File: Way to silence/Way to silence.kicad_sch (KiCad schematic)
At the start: 1 part, among them U1 ESP32-WROOM-32-N16

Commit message: [DRC] Working on BMS Sheet
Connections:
- no-connect marks 14 -> 17
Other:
- sheet Battery Management ports: added BAT, VIN, VOUT; removed none
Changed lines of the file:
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@@
   (paper "A4")
   (no_connect (at 120.65 71.12))
+  (no_connect (at 82.55 58.42))
   (no_connect (at 120.65 66.04))
   (no_connect (at 120.65 68.58))
@@
   (no_connect (at 199.39 55.88))
   (no_connect (at 176.53 90.17))
+  (no_connect (at 82.55 63.5))
   (no_connect (at 199.39 58.42))
   (no_connect (at 176.53 87.63))
+  (no_connect (at 82.55 60.96))
   (no_connect (at 199.39 66.04))
   (symbol (lib_id "power:PWR_FLAG") (at 177.8 25.4 0) (unit 1)
@@
       (effects (font (size 1.27 1.27)) (justify left top))
     )
-    (instances
+    (pin "VIN" bidirectional (at 82.55 58.42 180)
+      (effects (font (size 1.27 1.27)) (justify left))
+    )
+    (pin "VOUT" bidirectional (at 82.55 60.96 180)
+      (effects (font (size 1.27 1.27)) (justify left))
+    )
+    (pin "BAT" bidirectional (at 82.55 63.5 180)
+      (effects (font (size 1.27 1.27)) (justify left))
+    )
+    (instances

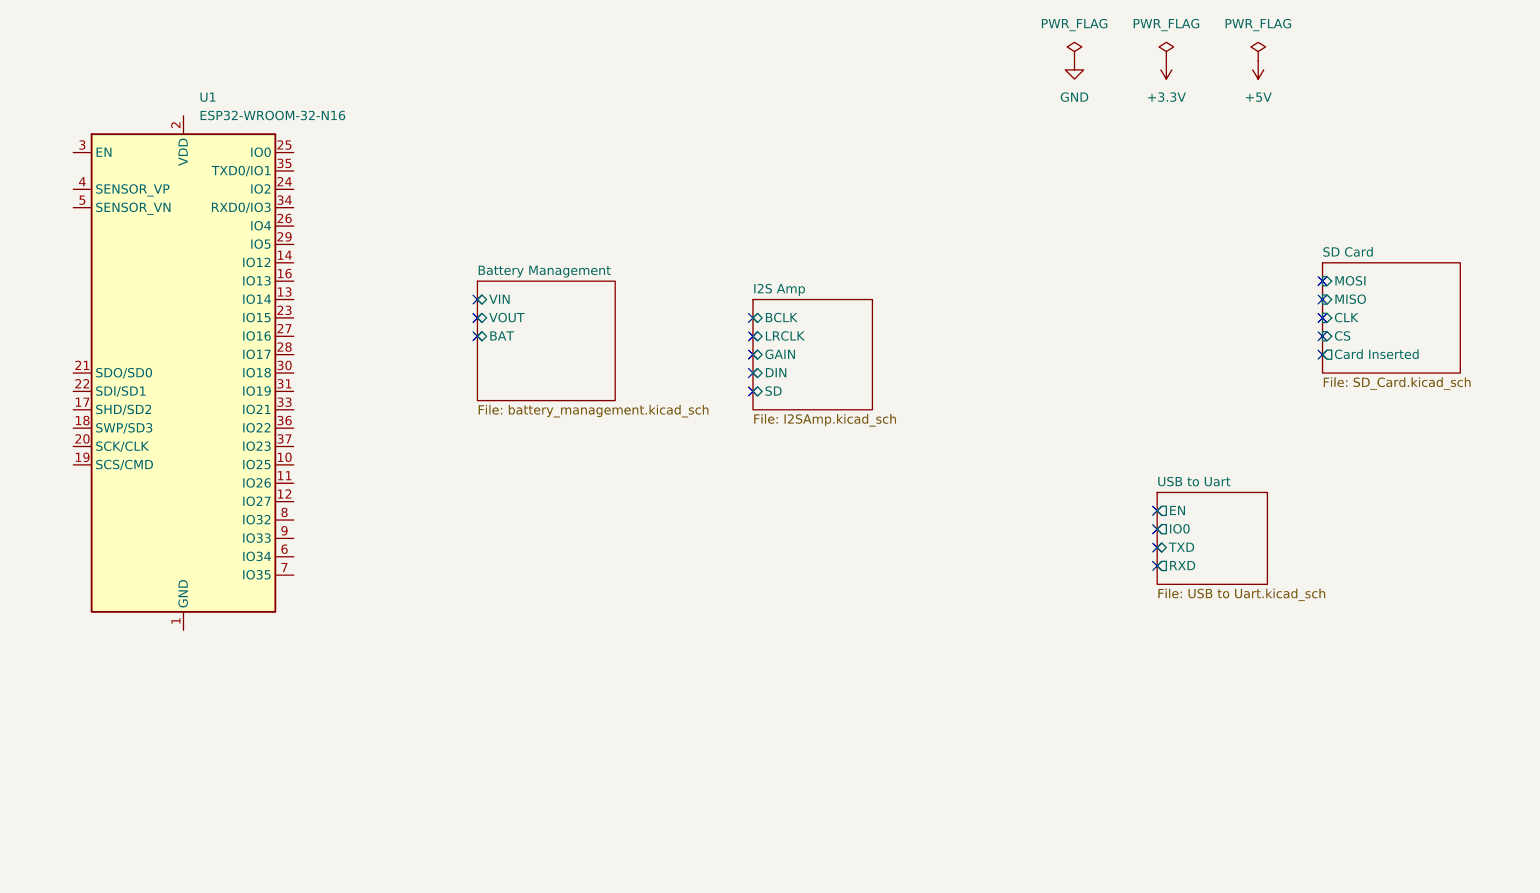
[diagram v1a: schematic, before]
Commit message: [ADD] Completed some connections in main sheet
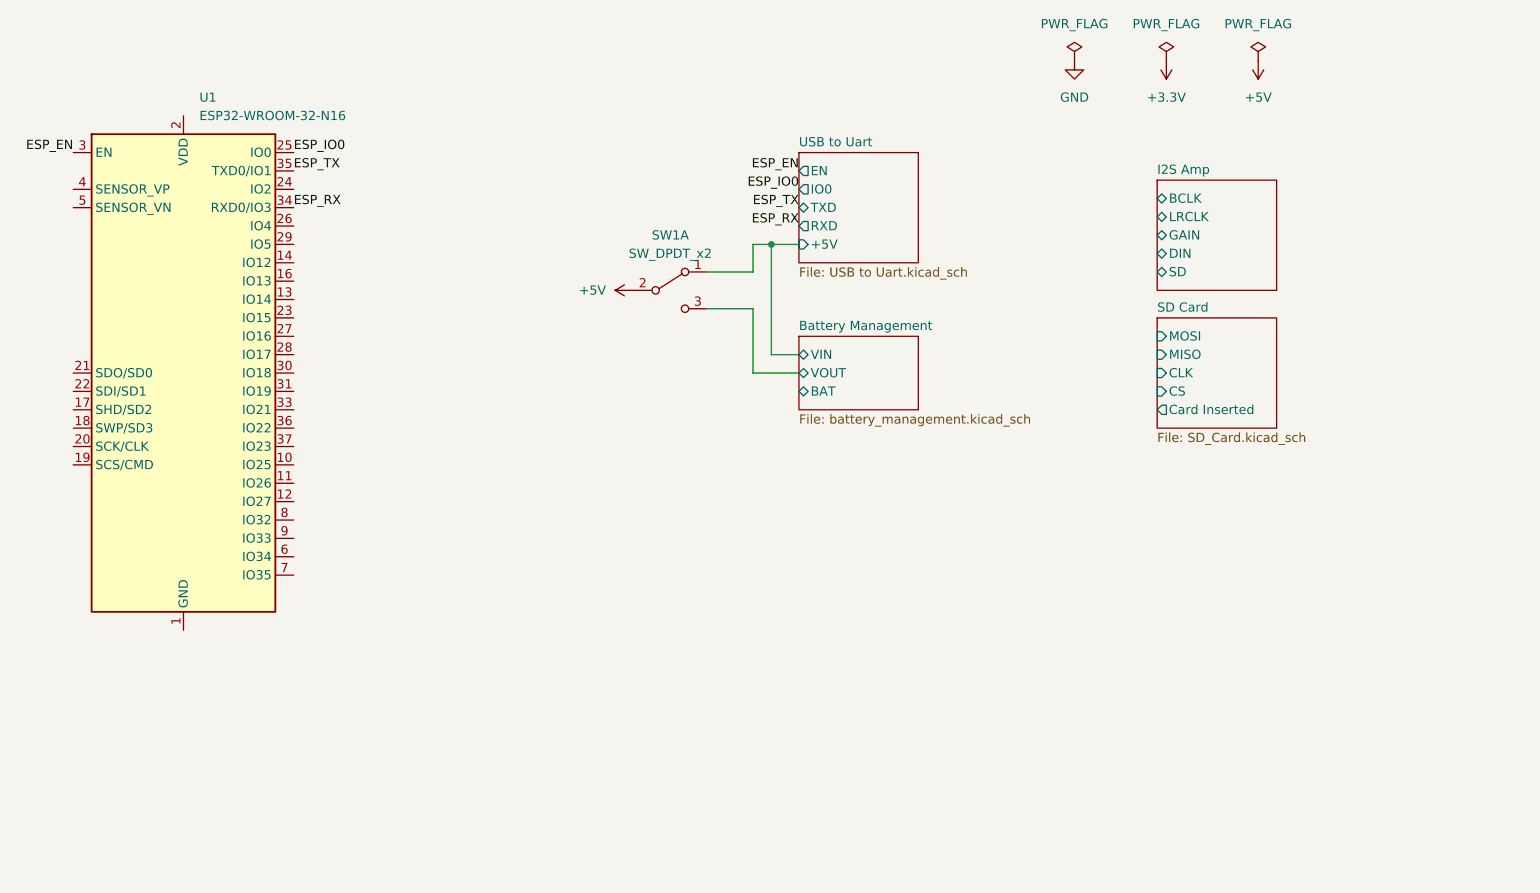
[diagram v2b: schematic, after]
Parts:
- added SW1: SW_DPDT_x2, symbol Way to silence:SW_DPDT_x2
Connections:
- net +5V: now also SW1.2 (B)
- net Battery Management/VIN: now also SW1.1 (A)
- net Battery Management/VOUT: now also SW1.3 (C)
- net ESP_IO0: now reaches U1.25 (IO0)
- net ESP_EN: now reaches U1.3 (EN)
- net ESP_RX: now reaches U1.34 (RXD0/IO3)
- net ESP_TX: now reaches U1.35 (TXD0/IO1)
- no-connect marks 17 -> 0
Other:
- sheet USB to Uart ports: added +5V; removed none

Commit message: [ADD] 3v3 Reg
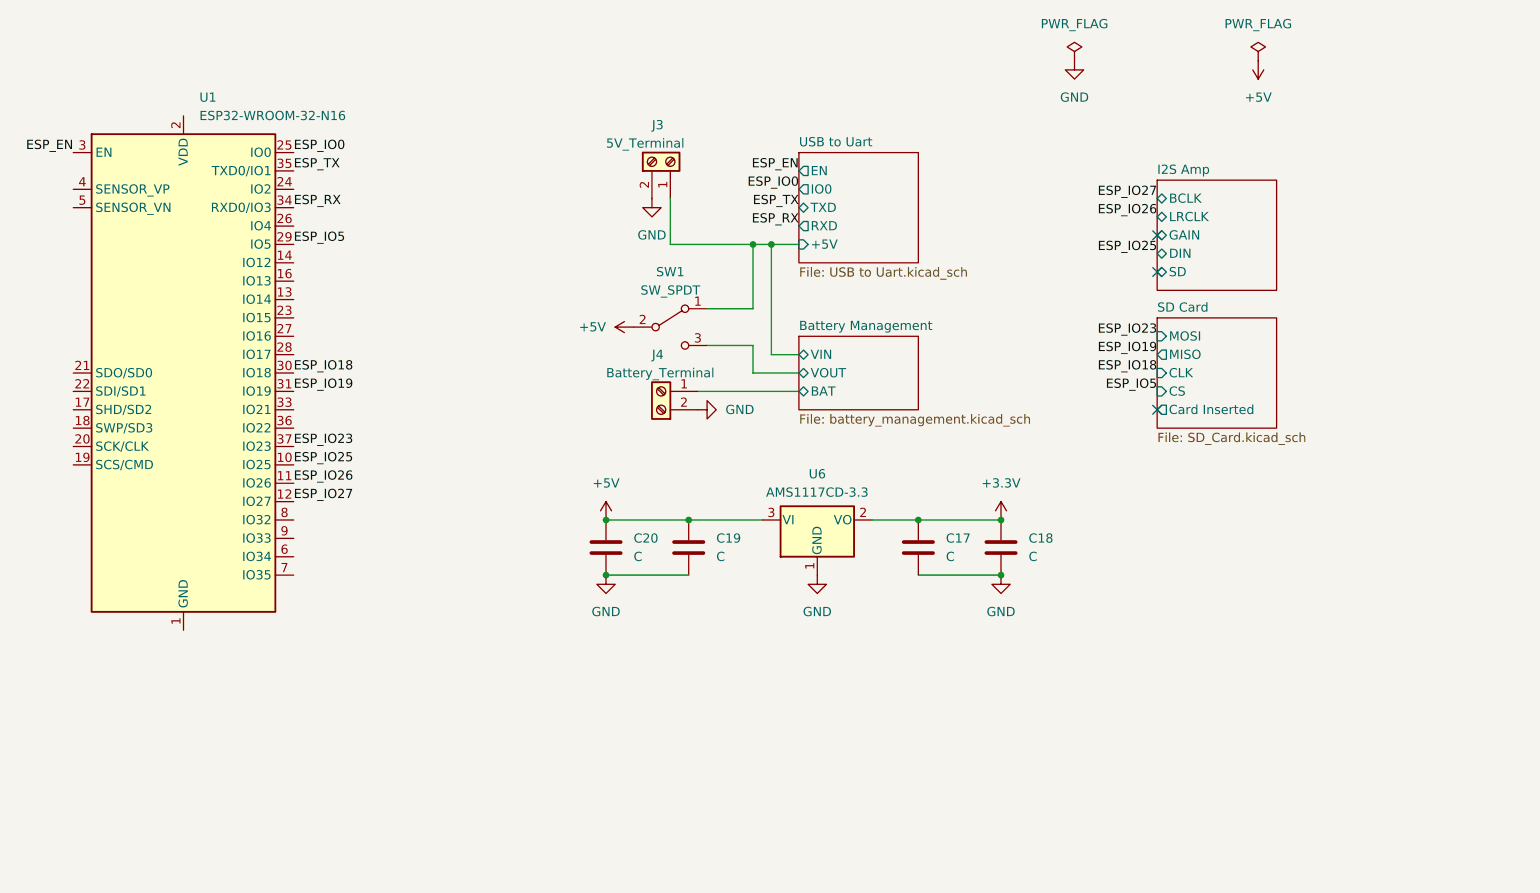
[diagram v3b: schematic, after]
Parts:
- removed SW1: SW_DPDT_x2, symbol Way to silence:SW_DPDT_x2
- added C17, C18, C19, C20: C, symbol Way to silence:C
- added J3: 5V_Terminal, symbol Way to silence:Screw_Terminal_01x02
- added J4: Battery_Terminal, symbol Way to silence:Screw_Terminal_01x02
- added SW1: SW_SPDT, symbol Way to silence:SW_SPDT
- added U6: AMS1117CD-3.3, Package_TO_SOT_SMD:TO-252-3_TabPin2, symbol Way to silence:AMS1117CD-3.3
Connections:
- net +3.3V: now also C17.2, C18.2, U6.2 (VO)
- net +5V: now also C19.2, C20.2, SW1.2 (B), U6.3 (VI)
- net Battery Management/BAT: now also J4.1 (Pin_1)
- net Battery Management/VIN: now also J3.1 (Pin_1), SW1.1 (A)
- net Battery Management/VOUT: now also SW1.3 (C)
- net GND: now also C17.1, C18.1, C19.1, C20.1, J3.2 (Pin_2), J4.2 (Pin_2), U6.1 (GND)
- net ESP_IO25: now reaches U1.10 (IO25)
- net ESP_IO26: now reaches U1.11 (IO26)
- net ESP_IO27: now reaches U1.12 (IO27)
- net ESP_IO5: now reaches U1.29 (IO5)
- net ESP_IO18: now reaches U1.30 (IO18)
- net ESP_IO19: now reaches U1.31 (IO19)
- net ESP_IO23: now reaches U1.37 (IO23)
- no-connect marks 0 -> 3

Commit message: [DRC] No errors
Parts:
- added D5, D6: LED, symbol Way to silence:LED
- added R19, R20: 1K, symbol Way to silence:R
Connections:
- net +3.3V: now also U1.2 (VDD), R19.2
- net GND: now also U1.1 (GND), U1.15 (GND), U1.38 (GND), U1.39 (GND), D5.1 (K), D6.1 (K)
- net ESP_IO2: now reaches U1.24 (IO2)
- net ESP_IO2: now also R20.2
- new net: D6.2 (A), R20.1
- new net: D5.2 (A), R19.1
- no-connect marks 3 -> 24
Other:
- note added: "Safe"

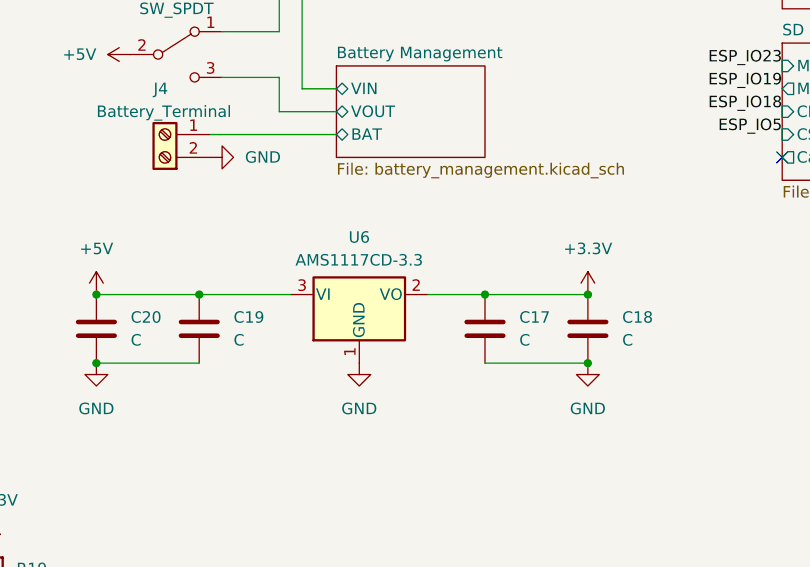
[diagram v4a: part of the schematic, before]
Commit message: [ADD] New reg footprint and datasheet
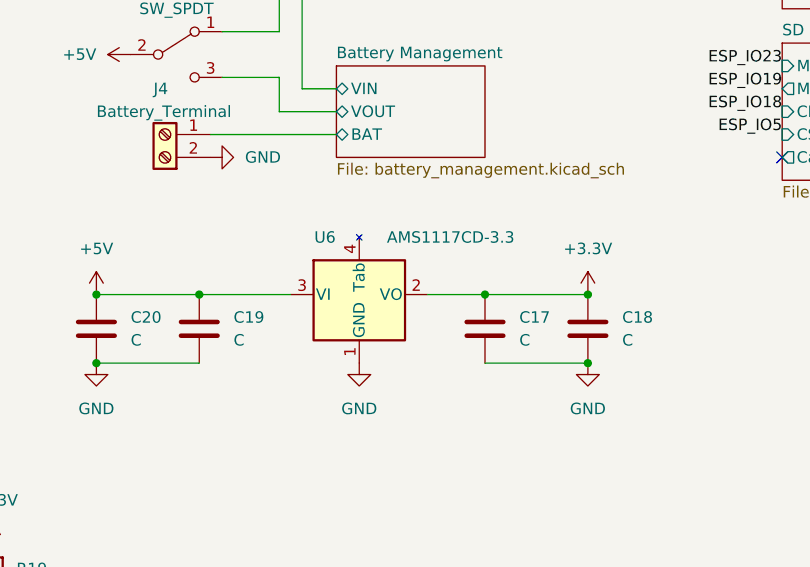
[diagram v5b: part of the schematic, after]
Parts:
- SW1: footprint (none) -> Way to silence:SW_SPDT; LCSC (none) -> C145861
- U6: LCSC (none) -> C347222
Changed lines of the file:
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@@
   (symbol (lib_id "Way to silence:AMS1117CD-3.3") (at 129.54 88.9 0) (unit 1)
     (in_bom yes) (on_board yes) (dnp no) (fields_autoplaced)
-    (property "Reference" "U6" (at 129.54 82.55 0)
+    (property "Reference" "U6" (at 125.73 82.55 0)
       (effects (font (size 1.27 1.27)))
     )
-    (property "Value" "AMS1117CD-3.3" (at 129.54 85.09 0)
+    (property "Value" "AMS1117CD-3.3" (at 139.7 82.55 0)
       (effects (font (size 1.27 1.27)))
     )
-    (property "Footprint" "Package_TO_SOT_SMD:TO-252-3_TabPin2" (at 129.54 82.55 0)
+    (property "Footprint" "Package_TO_SOT_SMD:TO-252-3_TabPin2" (at 130.81 66.04 0)
       (effects (font (size 1.27 1.27)) hide)
     )
-    (property "Datasheet" "http://www.advanced-monolithic.com/pdf/ds1117.pdf" (at 130.81 80.01 0)
+    (property "Datasheet" "https://datasheet.lcsc.com/lcsc/2110111730_UMW-Youtai-Semiconductor-Co---Ltd--AMS1117-3-3_C347222.pdf" (at 132.08 63.5 0)
+      (effects (font (size 1.27 1.27)) hide)
+    )
+    (property "LCSC" "C347222" (at 129.54 66.04 0)
       (effects (font (size 1.27 1.27)) hide)
     )
@@
     (pin "2")
     (pin "3")
+    (pin "4")
     (instances
       (project "Way to silence"
@@
       (effects (font (size 1.27 1.27)))
     )
-    (property "Footprint" "" (at 109.22 62.23 0)
+    (property "Footprint" "Way to silence:SW_SPDT" (at 107.95 48.26 0)
       (effects (font (size 1.27 1.27)) hide)
     )
-    (property "Datasheet" "~" (at 109.22 62.23 0)
+    (property "Datasheet" "https://github.com/juthomas/Way-To-Silence/blob/main/DataSheets/K3-1204D.pdf" (at 109.22 50.8 0)
       (effects (font (size 1.27 1.27)) hide)
     )
+    (property "LCSC" "C145861" (at 107.95 45.72 0)
+      (effects (font (size 1.27 1.27)) hide)
+    )

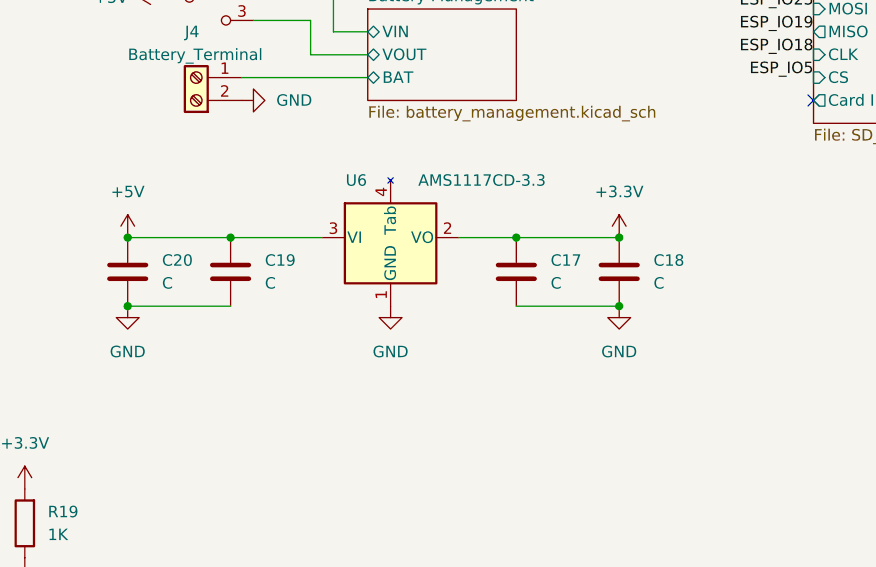
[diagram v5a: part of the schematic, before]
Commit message: [ADD] LSCS Parts and Footprints for BMS
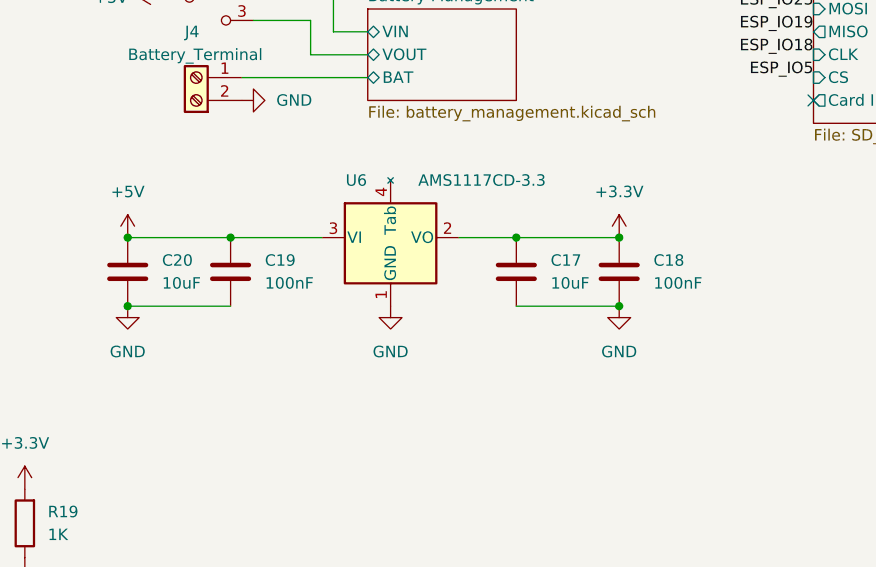
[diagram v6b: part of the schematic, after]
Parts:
- C17, C20: value C -> 10uF; footprint (none) -> Way to silence:C_0603_1608Metric
- C18, C19: value C -> 100nF; footprint (none) -> Way to silence:C_0603_1608Metric
- D5, D6: footprint (none) -> Way to silence:LED_0603; LCSC (none) -> C84263
- R19, R20: footprint (none) -> Way to silence:R_0603_1608Metric
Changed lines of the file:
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@@
       (effects (font (size 1.27 1.27)) (justify right))
     )
-    (property "Footprint" "" (at 77.978 120.65 0)
+    (property "Footprint" "Way to silence:R_0603_1608Metric" (at 77.978 120.65 0)
       (effects (font (size 1.27 1.27)) hide)
     )
@@
       (effects (font (size 1.27 1.27)) hide)
     )
-    (property "Datasheet" "https://datasheet.lcsc.com/lcsc/2110111730_UMW-Youtai-Semiconductor-Co---Ltd--AMS1117-3-3_C347222.pdf" (at 132.08 63.5 0)
+    (property "Datasheet" "http://www.advanced-monolithic.com/pdf/ds1117.pdf" (at 132.08 63.5 0)
       (effects (font (size 1.27 1.27)) hide)
     )
@@
       (effects (font (size 1.27 1.27)) hide)
     )
-    (property "Datasheet" "https://github.com/juthomas/Way-To-Silence/blob/main/DataSheets/K3-1204D.pdf" (at 109.22 50.8 0)
+    (property "Datasheet" "~" (at 109.22 50.8 0)
       (effects (font (size 1.27 1.27)) hide)
     )
@@
       (effects (font (size 1.27 1.27)) (justify right))
     )
-    (property "Value" "C" (at 147.32 93.98 90)
-      (effects (font (size 1.27 1.27)) (justify right))
-    )
-    (property "Footprint" "" (at 142.5448 88.9 90)
+    (property "Value" "10uF" (at 147.32 93.98 90)
+      (effects (font (size 1.27 1.27)) (justify right))
+    )
+    (property "Footprint" "Way to silence:C_0603_1608Metric" (at 142.5448 88.9 90)
       (effects (font (size 1.27 1.27)) hide)
     )
@@
       (effects (font (size 1.27 1.27)) (justify right))
     )
-    (property "Footprint" "" (at 76.2 128.27 0)
+    (property "Footprint" "Way to silence:LED_0603" (at 76.2 128.27 0)
       (effects (font (size 1.27 1.27)) hide)
     )
@@
       (effects (font (size 1.27 1.27)) hide)
     )
+    (property "LCSC" "C84263" (at 71.12 128.27 0)
+      (effects (font (size 1.27 1.27)) hide)
+    )
     (pin "1")
     (pin "2")
@@
       (effects (font (size 1.27 1.27)) (justify right))
     )
-    (property "Footprint" "" (at 88.9 128.27 0)
+    (property "Footprint" "Way to silence:LED_0603" (at 88.9 128.27 0)
       (effects (font (size 1.27 1.27)) hide)
     )
@@
       (effects (font (size 1.27 1.27)) hide)
     )
+    (property "LCSC" "C84263" (at 83.82 128.27 0)
+      (effects (font (size 1.27 1.27)) hide)
+    )
     (pin "1")
     (pin "2")
@@
       (effects (font (size 1.27 1.27)) (justify right))
     )
-    (property "Value" "C" (at 158.75 93.98 90)
-      (effects (font (size 1.27 1.27)) (justify right))
-    )
-    (property "Footprint" "" (at 153.9748 88.9 90)
+    (property "Value" "100nF" (at 158.75 93.98 90)
+      (effects (font (size 1.27 1.27)) (justify right))
+    )
+    (property "Footprint" "Way to silence:C_0603_1608Metric" (at 153.9748 88.9 90)
       (effects (font (size 1.27 1.27)) hide)
     )
@@
       (effects (font (size 1.27 1.27)) (justify right))
     )
-    (property "Footprint" "" (at 90.678 120.65 0)
+    (property "Footprint" "Way to silence:R_0603_1608Metric" (at 90.678 120.65 0)
       (effects (font (size 1.27 1.27)) hide)
     )
@@
       (effects (font (size 1.27 1.27)) (justify right))
     )
-    (property "Value" "C" (at 104.14 93.98 90)
-      (effects (font (size 1.27 1.27)) (justify right))
-    )
-    (property "Footprint" "" (at 99.3648 88.9 90)
+    (property "Value" "10uF" (at 104.14 93.98 90)
+      (effects (font (size 1.27 1.27)) (justify right))
+    )
+    (property "Footprint" "Way to silence:C_0603_1608Metric" (at 99.3648 88.9 90)
       (effects (font (size 1.27 1.27)) hide)
     )
@@
       (effects (font (size 1.27 1.27)) (justify right))
     )
-    (property "Value" "C" (at 115.57 93.98 90)
-      (effects (font (size 1.27 1.27)) (justify right))
-    )
-    (property "Footprint" "" (at 110.7948 88.9 90)
-      (effects (font (size 1.27 1.27)) hide)
-    )
+    (property "Value" "100nF" (at 115.57 93.98 90)
+      (effects (font (size 1.27 1.27)) (justify right))
+    )
+    (property "Footprint" "Way to silence:C_0603_1608Metric" (at 110.7948 88.9 90)
+      (effects (font (size 1.27 1.27)) hide)
+    )

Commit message: [ADD] References in readme
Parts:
- C17, C20: LCSC (none) -> C77041
- C18, C19: LCSC (none) -> C14663
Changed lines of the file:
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@@
+      (effects (font (size 1.27 1.27)) hide)
+    )
+    (property "LCSC" "C77041" (at 143.51 92.71 90)
       (effects (font (size 1.27 1.27)) hide)
     )
@@
     )
     (property "Datasheet" "~" (at 154.94 92.71 90)
+      (effects (font (size 1.27 1.27)) hide)
+    )
+    (property "LCSC" "C14663" (at 154.94 92.71 90)
       (effects (font (size 1.27 1.27)) hide)
     )
@@
       (effects (font (size 1.27 1.27)) hide)
     )
+    (property "LCSC" "C77041" (at 100.33 92.71 90)
+      (effects (font (size 1.27 1.27)) hide)
+    )
     (pin "1")
     (pin "2")
@@
       (effects (font (size 1.27 1.27)) hide)
     )
+    (property "LCSC" "C14663" (at 111.76 92.71 90)
+      (effects (font (size 1.27 1.27)) hide)
+    )

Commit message: [UPDT] Switch source
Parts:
- SW1: LCSC C145861 -> C319013
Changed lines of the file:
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@@
       (effects (font (size 1.27 1.27)) hide)
     )
-    (property "LCSC" "C145861" (at 107.95 45.72 0)
+    (property "LCSC" "C319013" (at 107.95 45.72 0)
       (effects (font (size 1.27 1.27)) hide)
     )
